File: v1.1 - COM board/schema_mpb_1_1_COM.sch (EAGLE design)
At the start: 2 parts, among them IC1 E73_2G4M04S, U1 ESP-WROOM-32

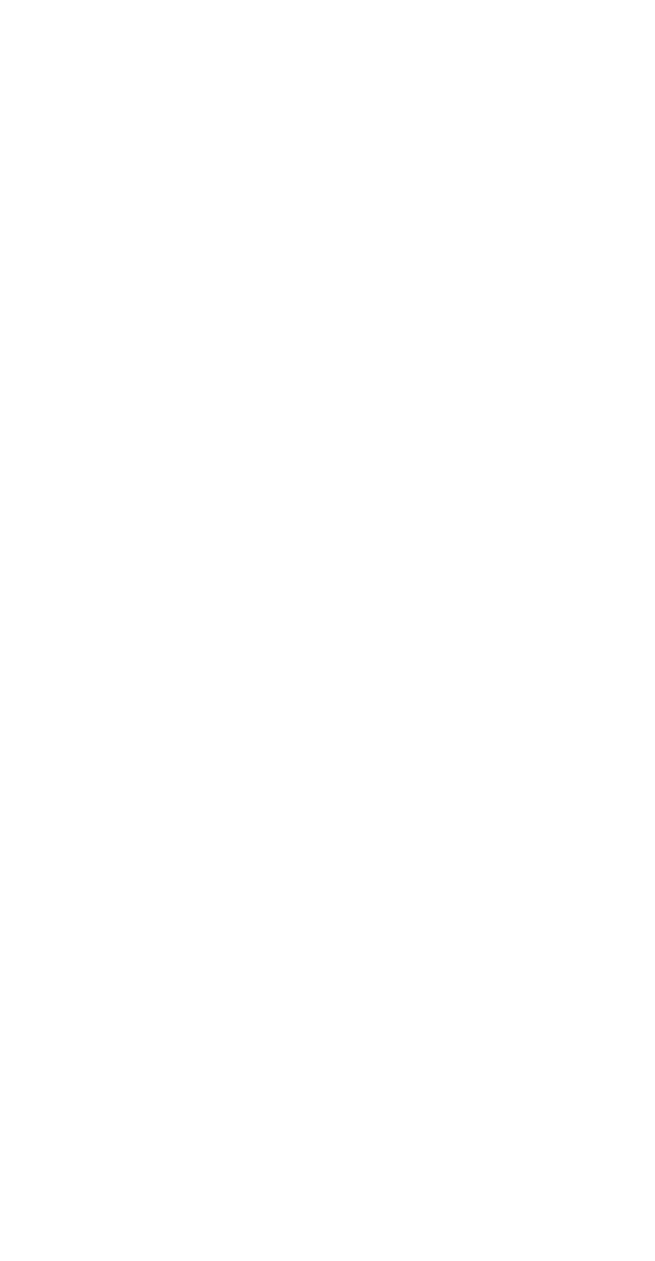
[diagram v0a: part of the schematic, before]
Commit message: Main board revisions
- Rerouted long tracks to other layers
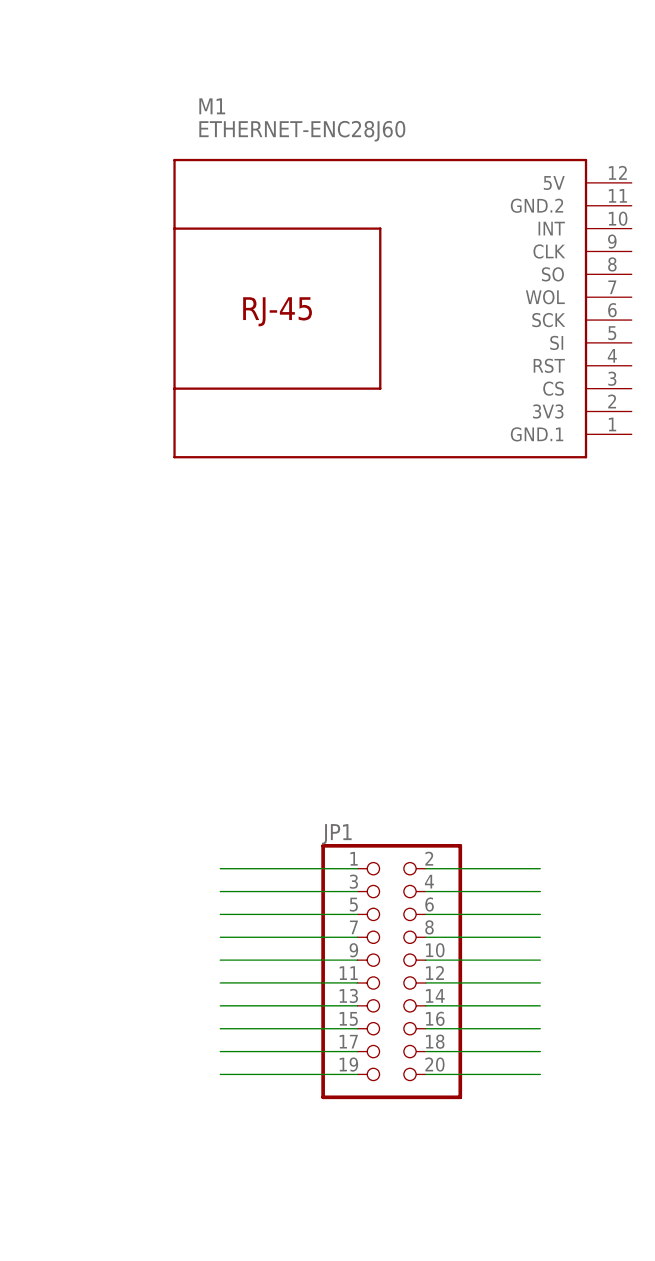
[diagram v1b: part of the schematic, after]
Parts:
- added JP1: (no value), pinhead:PINHD-2X10
- added M1: ETHERNET-ENC28J60, diy-modules:ETHERNET-ENC28J60
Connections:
- new net N$1: JP1.1
- new net N$10: JP1.19
- new net N$11: JP1.20
- new net N$12: JP1.18
- new net N$13: JP1.16
- new net N$14: JP1.14
- new net N$15: JP1.12
- new net N$16: JP1.10
- new net N$17: JP1.8
- new net N$18: JP1.6
- new net N$19: JP1.4
- new net N$2: JP1.3
- new net N$20: JP1.2
- new net N$3: JP1.5
- new net N$4: JP1.7
- new net N$5: JP1.9
- new net N$6: JP1.11
- new net N$7: JP1.13
- new net N$8: JP1.15
- new net N$9: JP1.17
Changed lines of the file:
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@@
 <part name="IC1" library="E73-2G4M04S" deviceset="E73_2G4M04S" device=""/>
 <part name="U1" library="esp32" deviceset="ESP-WROOM-32" device=""/>
+<part name="M1" library="diy-modules" deviceset="ETHERNET-ENC28J60" device=""/>
+<part name="JP1" library="pinhead" library_urn="urn:adsk.eagle:library:325" deviceset="PINHD-2X10" device="" package3d_urn="urn:adsk.eagle:package:22405/2"/>
 </parts>
 <sheets>
@@
 <instance part="IC1" gate="G$1" x="167.64" y="182.88"/>
 <instance part="U1" gate="G$1" x="165.1" y="91.44"/>
+<instance part="M1" gate="G$1" x="276.86" y="180.34"/>
+<instance part="JP1" gate="A" x="274.32" y="109.22"/>
 </instances>
 <busses>
 </busses>
 <nets>
+<net name="N$1" class="0">
+<segment>
+<pinref part="JP1" gate="A" pin="1"/>
+<wire x1="271.78" y1="119.38" x2="256.54" y2="119.38" width="0.1524" layer="91"/>
+</segment>
+</net>
+<net name="N$2" class="0">
+<segment>
+<pinref part="JP1" gate="A" pin="3"/>
+<wire x1="271.78" y1="116.84" x2="256.54" y2="116.84" width="0.1524" layer="91"/>
+</segment>
+</net>
+<net name="N$3" class="0">
+<segment>
+<pinref part="JP1" gate="A" pin="5"/>
+<wire x1="271.78" y1="114.3" x2="256.54" y2="114.3" width="0.1524" layer="91"/>
+</segment>
+</net>
+<net name="N$4" class="0">
+<segment>
+<pinref part="JP1" gate="A" pin="7"/>
+<wire x1="271.78" y1="111.76" x2="256.54" y2="111.76" width="0.1524" layer="91"/>
+</segment>
+</net>
+<net name="N$5" class="0">
+<segment>
+<pinref part="JP1" gate="A" pin="9"/>
+<wire x1="271.78" y1="109.22" x2="256.54" y2="109.22" width="0.1524" layer="91"/>
+</segment>
+</net>
+<net name="N$6" class="0">
+<segment>
+<pinref part="JP1" gate="A" pin="11"/>
+<wire x1="271.78" y1="106.68" x2="256.54" y2="106.68" width="0.1524" layer="91"/>
+</segment>
+</net>
+<net name="N$7" class="0">
+<segment>
+<pinref part="JP1" gate="A" pin="13"/>
+<wire x1="271.78" y1="104.14" x2="256.54" y2="104.14" width="0.1524" layer="91"/>
+</segment>
+</net>
+<net name="N$8" class="0">
+<segment>
+<pinref part="JP1" gate="A" pin="15"/>
+<wire x1="271.78" y1="101.6" x2="256.54" y2="101.6" width="0.1524" layer="91"/>
+</segment>
+</net>
+<net name="N$9" class="0">
+<segment>
+<pinref part="JP1" gate="A" pin="17"/>
+<wire x1="271.78" y1="99.06" x2="256.54" y2="99.06" width="0.1524" layer="91"/>
+</segment>
+</net>
+<net name="N$10" class="0">
+<segment>
+<pinref part="JP1" gate="A" pin="19"/>
+<wire x1="271.78" y1="96.52" x2="256.54" y2="96.52" width="0.1524" layer="91"/>
+</segment>
+</net>
+<net name="N$11" class="0">
+<segment>
+<pinref part="JP1" gate="A" pin="20"/>
+<wire x1="279.4" y1="96.52" x2="292.1" y2="96.52" width="0.1524" layer="91"/>
+</segment>
+</net>
+<net name="N$12" class="0">
+<segment>
+<pinref part="JP1" gate="A" pin="18"/>
+<wire x1="279.4" y1="99.06" x2="292.1" y2="99.06" width="0.1524" layer="91"/>
+</segment>
+</net>
+<net name="N$13" class="0">
+<segment>
+<pinref part="JP1" gate="A" pin="16"/>
+<wire x1="279.4" y1="101.6" x2="292.1" y2="101.6" width="0.1524" layer="91"/>
+</segment>
+</net>
+<net name="N$14" class="0">
+<segment>
+<pinref part="JP1" gate="A" pin="14"/>
+<wire x1="279.4" y1="104.14" x2="292.1" y2="104.14" width="0.1524" layer="91"/>
+</segment>
+</net>
+<net name="N$15" class="0">
+<segment>
+<pinref part="JP1" gate="A" pin="12"/>
+<wire x1="279.4" y1="106.68" x2="292.1" y2="106.68" width="0.1524" layer="91"/>
+</segment>
+</net>
+<net name="N$16" class="0">
+<segment>
+<pinref part="JP1" gate="A" pin="10"/>
+<wire x1="279.4" y1="109.22" x2="292.1" y2="109.22" width="0.1524" layer="91"/>
+</segment>
+</net>
+<net name="N$17" class="0">
+<segment>
+<pinref part="JP1" gate="A" pin="8"/>
+<wire x1="279.4" y1="111.76" x2="292.1" y2="111.76" width="0.1524" layer="91"/>
+</segment>
+</net>
+<net name="N$18" class="0">
+<segment>
+<pinref part="JP1" gate="A" pin="6"/>
+<wire x1="279.4" y1="114.3" x2="292.1" y2="114.3" width="0.1524" layer="91"/>
+</segment>
+</net>
+<net name="N$19" class="0">
+<segment>
+<pinref part="JP1" gate="A" pin="4"/>
+<wire x1="279.4" y1="116.84" x2="292.1" y2="116.84" width="0.1524" layer="91"/>
+</segment>
+</net>
+<net name="N$20" class="0">
+<segment>
+<pinref part="JP1" gate="A" pin="2"/>
+<wire x1="279.4" y1="119.38" x2="292.1" y2="119.38" width="0.1524" layer="91"/>
+</segment>
+</net>
 </nets>
 </sheet>
@@
 will not be understood (or retained) with this version.
 </note>
+<note version="8.3" severity="warning">
+Since Version 8.3, EAGLE supports the association of 3D packages
+with devices in libraries, schematics, and board files. Those 3D
+packages will not be understood (or retained) with this version.
+</note>
 </compatibility>

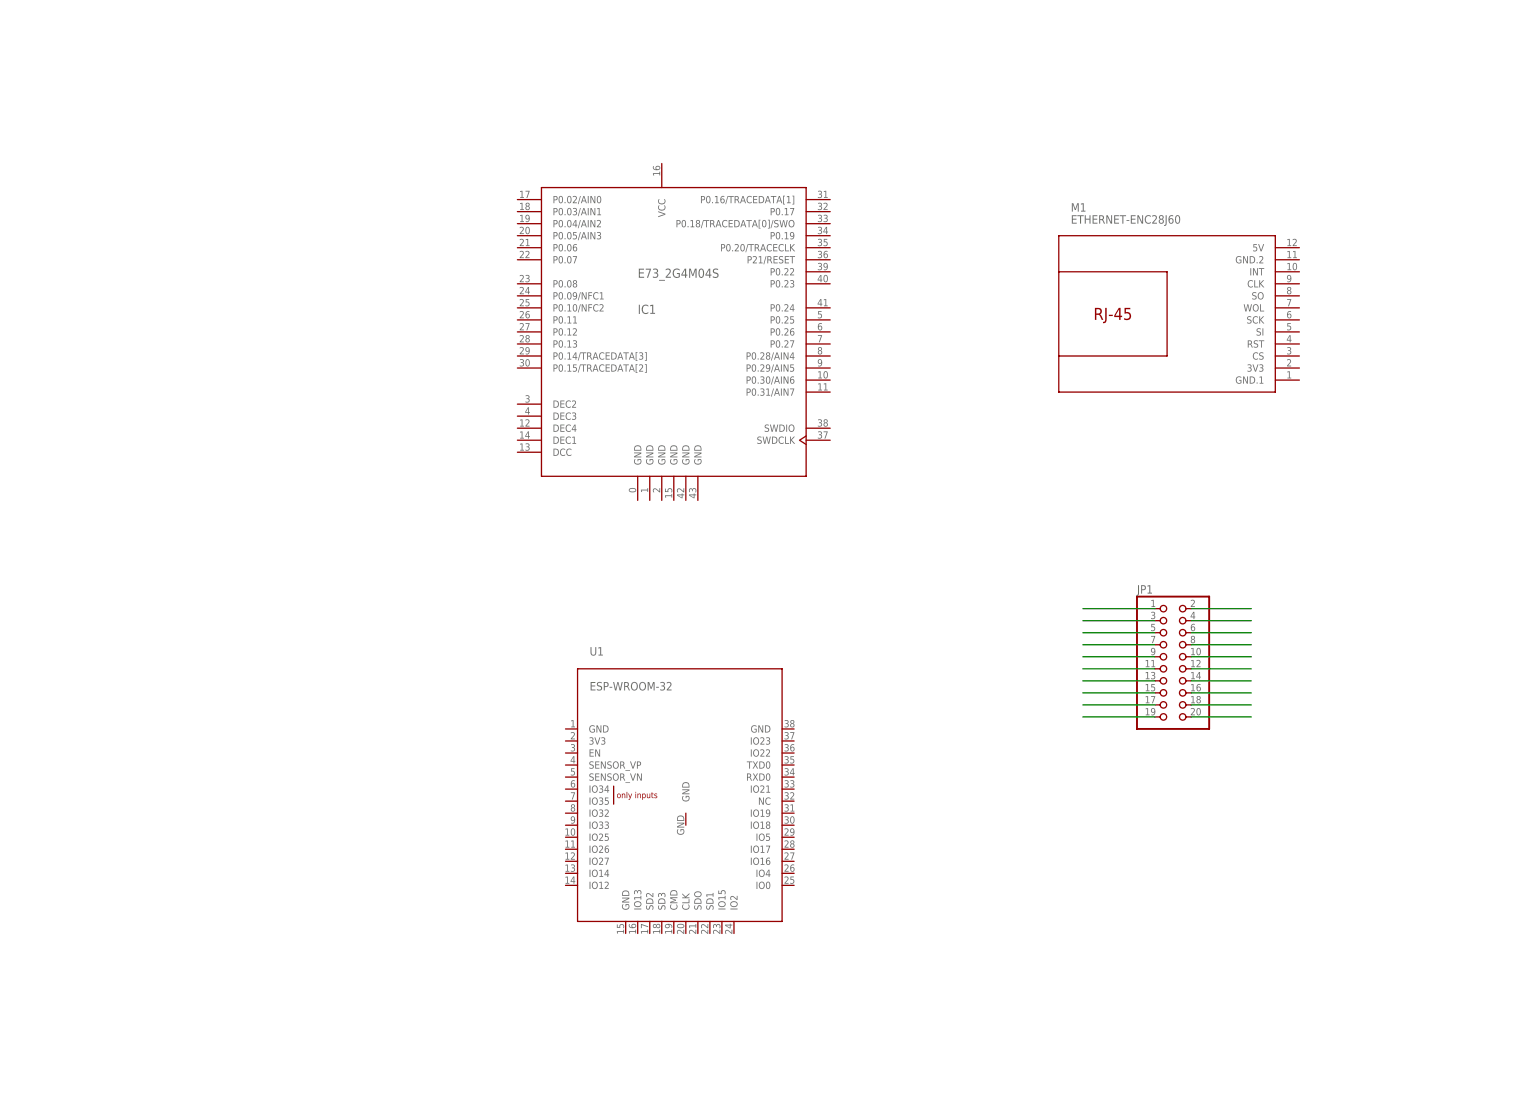
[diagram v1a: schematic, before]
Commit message: Main board
- Tidied tracks
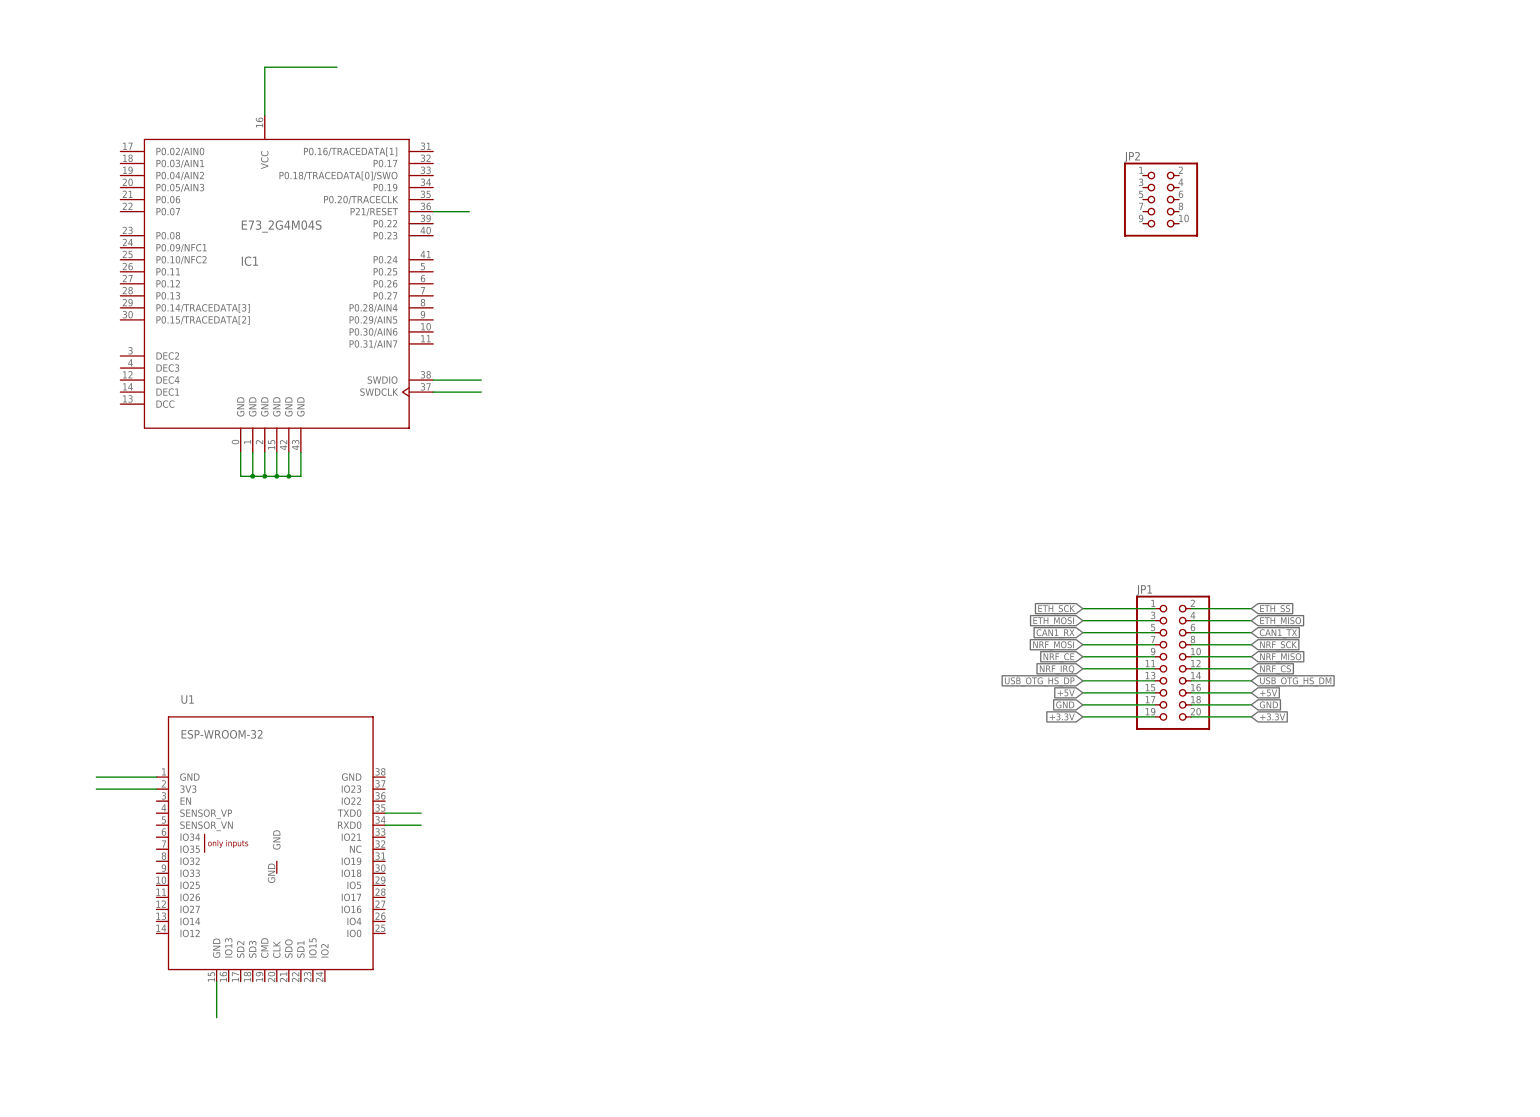
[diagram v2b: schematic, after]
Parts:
- removed M1: ETHERNET-ENC28J60, diy-modules:ETHERNET-ENC28J60
- added JP2: (no value), pinhead:PINHD-2X5
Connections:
- net N$1 renamed ETH_SCK
- net N$14 renamed USB_OTG_HS_DM
- net N$15 renamed NRF_CS
- net N$16 renamed NRF_MISO
- net N$17 renamed NRF_SCK
- net N$18 renamed CAN1_TX
- net N$19 renamed ETH_MISO
- net N$2 renamed ETH_MOSI
- net N$20 renamed ETH_SS
- net N$3 renamed CAN1_RX
- net N$4 renamed NRF_MOSI
- net N$5 renamed NRF_CE
- net N$6 renamed NRF_IRQ
- net N$7 renamed USB_OTG_HS_DP
- removed net N$11: JP1.20
- removed net N$12: JP1.18
- removed net N$13: JP1.16
- new net +3.3V: JP1.19, JP1.20
- new net +5V: JP1.15, JP1.16
- new net GND: JP1.17, JP1.18
- new net N$1: U1.GND@1
- new net N$2: U1.3V3
- new net N$3: U1.TXD0
- new net N$4: U1.RXD0
- new net N$5: U1.GND@15
- new net N$6: IC1.GND@1, IC1.GND@2, IC1.GND@3, IC1.GND@4, IC1.GND@5, IC1.GND@6
- new net N$7: IC1.SWDIO
- net N$10: now also IC1.P21/RESET; no longer JP1.19
- net N$8: now also IC1.SWDCLK; no longer JP1.15
- net N$9: now also IC1.VCC@1; no longer JP1.17
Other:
- moved on the sheet: IC1, U1
